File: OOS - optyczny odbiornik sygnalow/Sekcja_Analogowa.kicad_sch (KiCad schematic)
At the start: 52 parts, among them J1 Conn_01x02_Socket, J2 Conn_01x02_Socket, J3 Conn_01x02_Socket, J4 Conn_01x02_Socket, J5 Conn_Coaxial, U1 OPA300AIDBVR, U2 OPA300AIDBVR

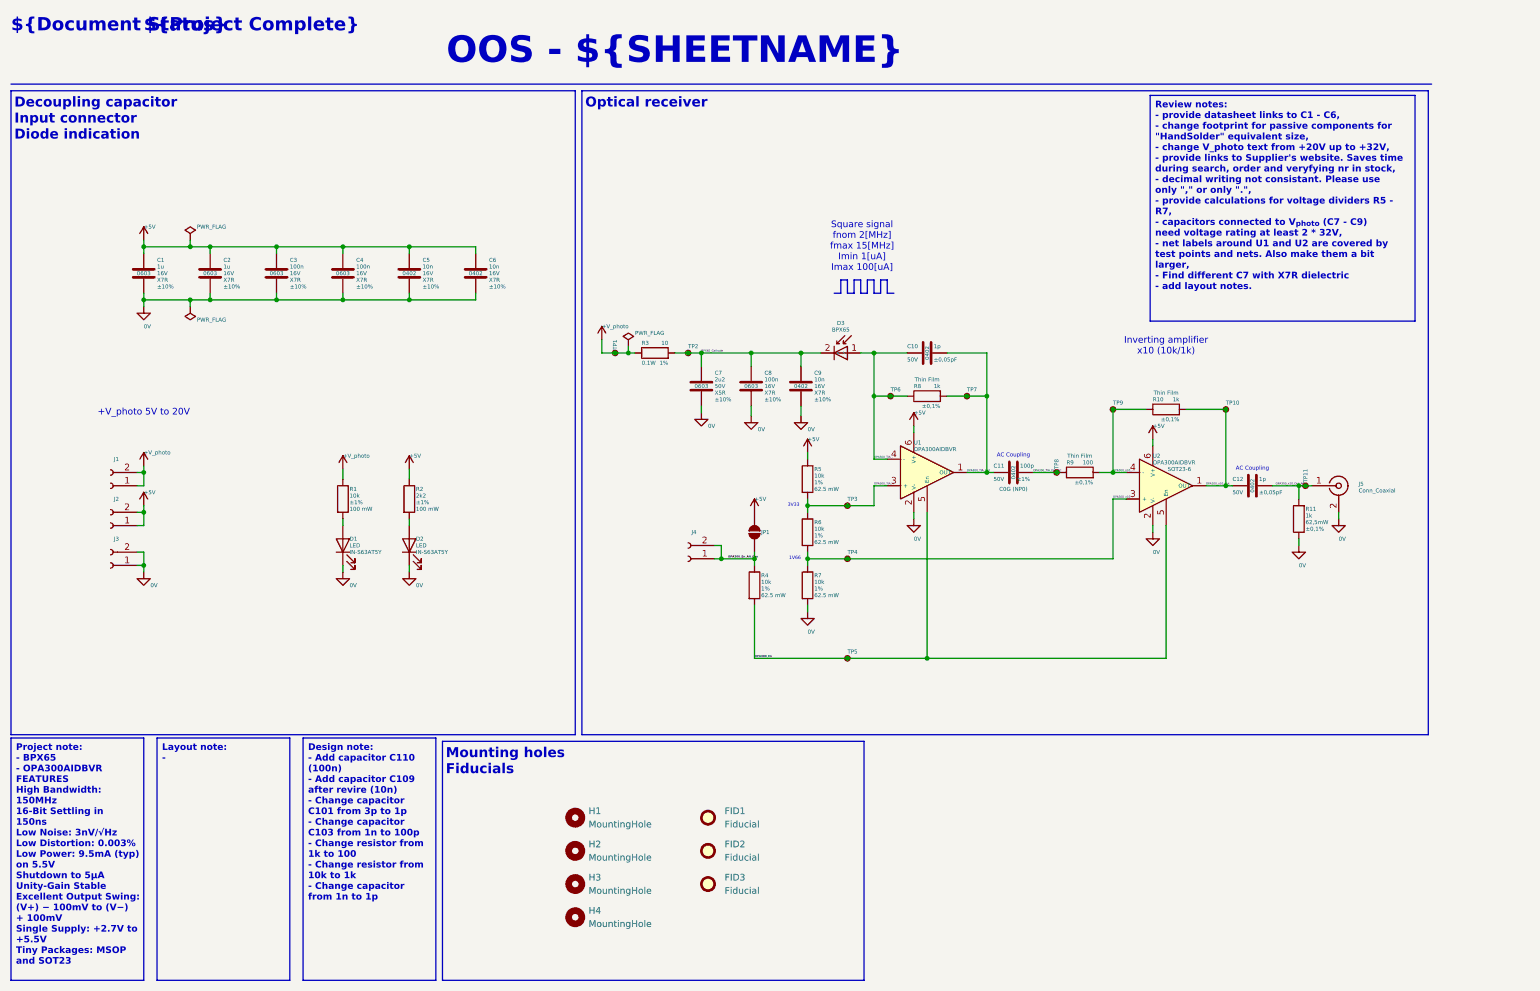
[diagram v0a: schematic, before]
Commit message: Solved points from review on page OOS - Analog
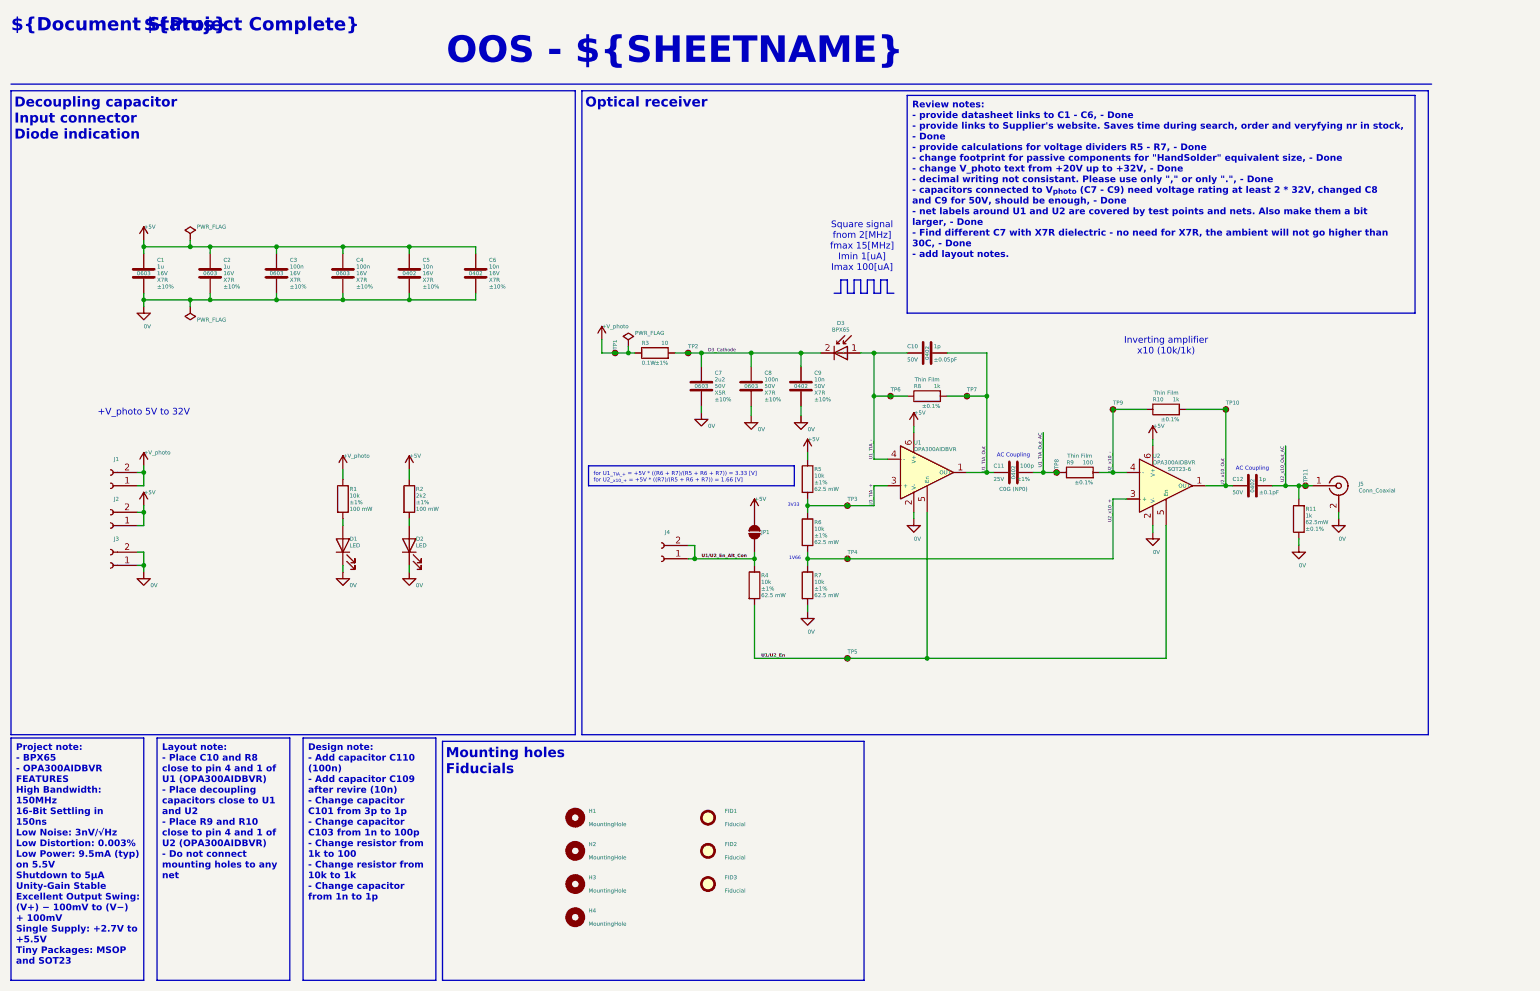
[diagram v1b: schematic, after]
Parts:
- C1, C2: footprint Capacitor_SMD:C_0603_1608Metric -> Capacitor_SMD:C_0603_1608Metric_Pad1.08x0.95mm_HandSolder; MPN (none) -> CC0603KRX7R7BB105; MPN after review C0603C105K4RACTU -> (none); Supplier Link (none) -> https://www.tme.eu/pl/details/cc0603krx7r7bb105/kondensator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
- C10: footprint Capacitor_SMD:C_0402_1005Metric -> Capacitor_SMD:C_0402_1005Metric_Pad0.74x0.62mm_HandSolder; MPN (none) -> GCM1555C1H1R0BA16D; MPN after review GJM1555C1H1R0WB01D -> (none); MPN before review GJM1555C1H3R0WB01D -> (none); Supplier Link (none) -> https://www.tme.eu/pl/details/gcm1555c1h1r0ba16d/kondensato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; Tolerance ±0,05pF -> ±0.05pF
- C11: footprint Capacitor_SMD:C_0402_1005Metric -> Capacitor_SMD:C_0402_1005Metric_Pad0.74x0.62mm_HandSolder; MPN (none) -> GRM0225C1E101GA02L; MPN after review GCM1555C1H101FA16D -> (none); MPN before review GCM1555C1H102FA16 -> (none); Supplier Link (none) -> https://www.tme.eu/pl/details/grm0225c1e101ga02l/kondensato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; Voltage Rating 50V -> 25V
- C12: footprint Capacitor_SMD:C_0402_1005Metric -> Capacitor_SMD:C_0402_1005Metric_Pad0.74x0.62mm_HandSolder; MPN (none) -> GCM1555C1H1R0BA16D; MPN after review GJM1555C1H1R0WB01D -> (none); MPN before review GCM1555C1H102FA16 -> (none); Supplier Link (none) -> https://www.tme.eu/pl/details/gcm1555c1h1r0ba16d/kondensato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; Tolerance ±0,05pF -> ±0.1pF
- C3, C4: footprint Capacitor_SMD:C_0603_1608Metric -> Capacitor_SMD:C_0603_1608Metric_Pad1.08x0.95mm_HandSolder; MPN (none) -> CL10B104KO8WPNC; MPN after review EMK108B7104KA-T -> (none); Supplier Link (none) -> https://www.tme.eu/pl/details/cl10b104ko8wpnc/kondensatory-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
- C5, C6: footprint Capacitor_SMD:C_0402_1005Metric -> Capacitor_SMD:C_0402_1005Metric_Pad0.74x0.62mm_HandSolder; MPN (none) -> CL05B103KO5NNNC; MPN after review CL05B103KO5NNNC -> (none); Supplier Link (none) -> https://www.tme.eu/pl/details/cl05b103ko5nnnc/kondensatory-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
- C7: footprint Capacitor_SMD:C_0603_1608Metric -> Capacitor_SMD:C_0603_1608Metric_Pad1.08x0.95mm_HandSolder; MPN (none) -> GRT188R61H225KE13D; MPN after review LMK107BJ225KA-T -> (none); Supplier NA -> Mouser; Supplier Link (none) -> https://www.tme.eu/pl/details/grt188r61h225ke13d/kondensato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
- C8: footprint Capacitor_SMD:C_0603_1608Metric -> Capacitor_SMD:C_0603_1608Metric_Pad1.08x0.95mm_HandSolder; MPN (none) -> CGA3E2X7R1H104KAA; MPN after review EMK108B7104KA-T -> (none); Supplier Link (none) -> https://www.tme.eu/pl/details/cga3e2x7r1h104kaa/kondensator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; Voltage Rating 16V -> 50V
- C9: footprint Capacitor_SMD:C_0402_1005Metric -> Capacitor_SMD:C_0402_1005Metric_Pad0.74x0.62mm_HandSolder; MPN (none) -> CL05B103KB5NNND; MPN after review CL05B103KO5NNNC -> (none); Supplier Link (none) -> https://www.tme.eu/pl/details/cl05b103kb5nnnd/kondensatory-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; Voltage Rating 16V -> 50V
- D1, D2: footprint Diode_SMD:D_0603_1608Metric -> Diode_SMD:D_0603_1608Metric_Pad1.05x0.95mm_HandSolder; MPN IN-S63AT5Y -> LTST-C191KGKT; Supplier Link (none) -> https://www.tme.eu/pl/details/ltst-c191kgkt/diody-led-smd-k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
- D3: MPN (none) -> BPX65; Supplier Link (none) -> https://www.tme.eu/pl/details/bpx65/fotodiody/ams-osram/bpx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
- J5: MPN (none) -> R-128; Package (none) -> THT; Supplier Link (none) -> https://www.tme.eu/pl/details/r-128/zlacza-bnc/hongkong-xin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
- R1: footprint Resistor_SMD:R_0603_1608Metric -> Resistor_SMD:R_0603_1608Metric_Pad0.98x0.95mm_HandSolder; MPN RC0603FR-0710KL -> RC0603FR-0710K; Supplier Link (none) -> https://www.tme.eu/pl/details/rc0603fr-0710k/rezystory-smd/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
- R10: footprint Resistor_SMD:R_0402_1005Metric -> Resistor_SMD:R_0402_1005Metric_Pad0.72x0.64mm_HandSolder; MPN (none) -> RT0402BRD071KL; MPN after review RT0402BRD071KL -> (none); MPN before review RT0402BRD0710KL -> (none); Power Rating 62,5mW -> 62.5mW; Supplier (none) -> TME; Supplier Link (none) -> https://www.tme.eu/pl/details/rt0402brd071kl/rezystory-smd/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; Tolerance ±0,1% -> ±0.1%
- R11, R8: footprint Resistor_SMD:R_0402_1005Metric -> Resistor_SMD:R_0402_1005Metric_Pad0.72x0.64mm_HandSolder; MPN (none) -> RT0402BRD071KL; MPN after review RT0402BRD071KL -> (none); Power Rating 62,5mW -> 62.5mW; Supplier (none) -> TME; Supplier Link (none) -> https://www.tme.eu/pl/details/rt0402brd071kl/rezystory-smd/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; Tolerance ±0,1% -> ±0.1%
- R2: footprint Resistor_SMD:R_0603_1608Metric -> Resistor_SMD:R_0603_1608Metric_Pad0.98x0.95mm_HandSolder; MPN RT0603FRE072K2L -> AC0603FR-072K2L; Supplier Link (none) -> https://www.tme.eu/pl/details/ac0603fr-072k2l/rezystory-smd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; Voltage Rating (none) -> 75V
- R3: footprint Resistor_SMD:R_0603_1608Metric -> Resistor_SMD:R_0603_1608Metric_Pad0.98x0.95mm_HandSolder; MPN (none) -> RCA060310R0FKEA; Supplier Link (none) -> https://www.tme.eu/pl/details/rca060310r0fkea/rezystory-smd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; Tolerance 1% -> ±1%; Voltage Rating 75 V -> 75V
- R4, R5, R6, R7: footprint Resistor_SMD:R_0402_1005Metric -> Resistor_SMD:R_0402_1005Metric_Pad0.72x0.64mm_HandSolder; MPN (none) -> WR04X1002FTL; MPN after review RC0603JR-13100KL -> (none); Supplier Link (none) -> https://www.tme.eu/pl/details/wr04x1002ftl/rezystory-smd/wa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; Tolerance 1% -> ±1%
- R9: footprint Resistor_SMD:R_0402_1005Metric -> Resistor_SMD:R_0402_1005Metric_Pad0.72x0.64mm_HandSolder; MPN (none) -> ERA2AEB101X; MPN after review ERA2AEB101X -> (none); MPN before review RT0402BRD071KL -> (none); Power Rating 62,5mW -> 62.5mW; Supplier Link (none) -> https://www.tme.eu/pl/details/era2aeb101x/rezystory-smd/pan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; Tolerance ±0,1% -> ±0.1%; Voltage Rating 100V -> 50V
- U1, U2: MPN (none) -> OPA300AIDBVR; Supplier Link (none) -> https://www.tme.eu/pl/details/opa300aidbvr/wzmacniacze-oper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
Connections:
- net BPX65_Cathode renamed D3_Cathode
- net OPA300_En renamed U1/U2_En
- net OPA300_En_Alt_Con renamed U1/U2_En_Alt_Con
- net OPA300_TIA_+ renamed U1_TIA_+
- net OPA300_TIA_- renamed U1_TIA_-
- net OPA300_TIA_Out renamed U1_TIA_Out
- net OPA300_TIA_Out_AC renamed U1_TIA_Out_AC
- net OPA300_x10_+ renamed U2_x10_+
- net OPA300_x10_- renamed U2_x10_-
- net OPA300_x10_Out renamed U2_x10_Out
- net OPA300_x10_Out_AC renamed U2_x10_Out_AC
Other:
- note added: "+V_photo 5V to 32V"
- note removed: "+V_photo 5V to 20V"
- moved on the sheet: J4
